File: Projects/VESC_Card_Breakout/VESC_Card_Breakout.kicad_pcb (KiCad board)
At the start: 2 copper layers, 9 parts, among them P1 USB_OTG, P2 CONN_01X02, P3 CONN_01X04, P4 EC90_Flat, P5 CONN_01X02, P6 AMP17614426-2_EDGE, P7 CONN_01X06

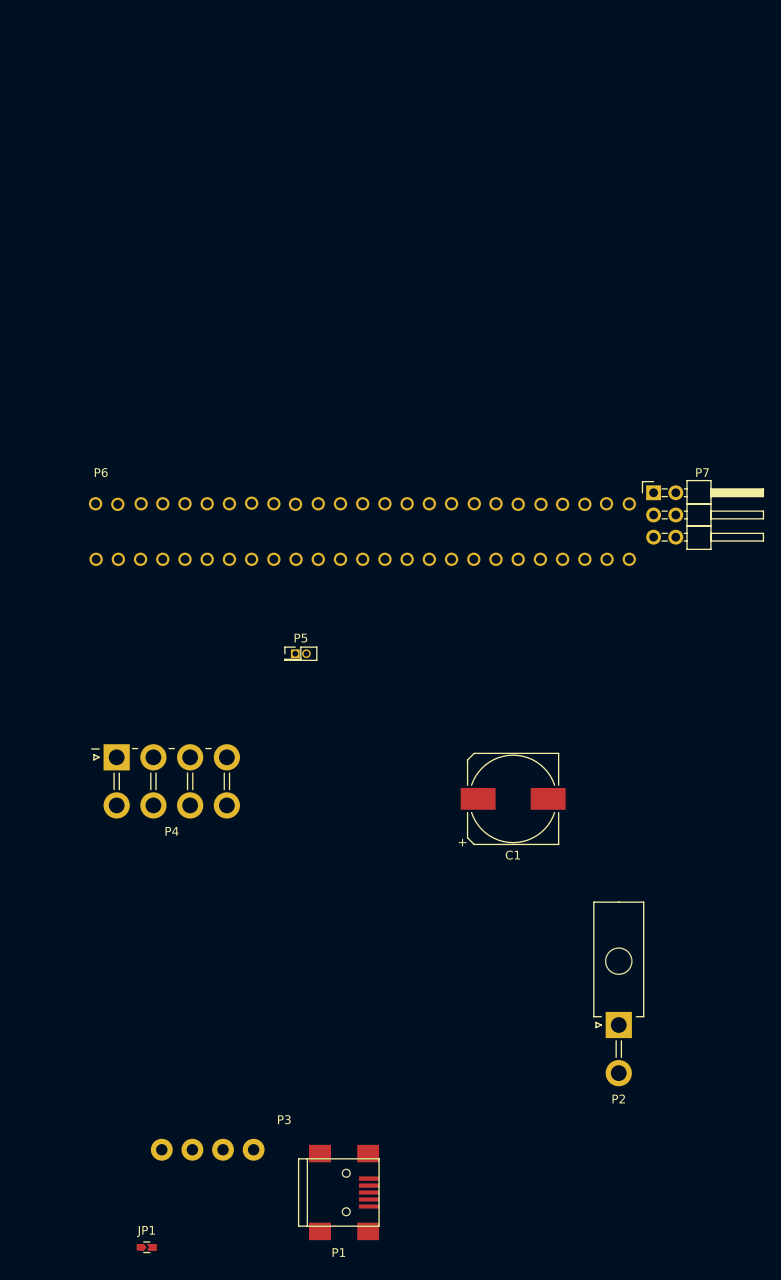
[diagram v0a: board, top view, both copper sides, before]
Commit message: Connected all for VESC_Card_Breakout
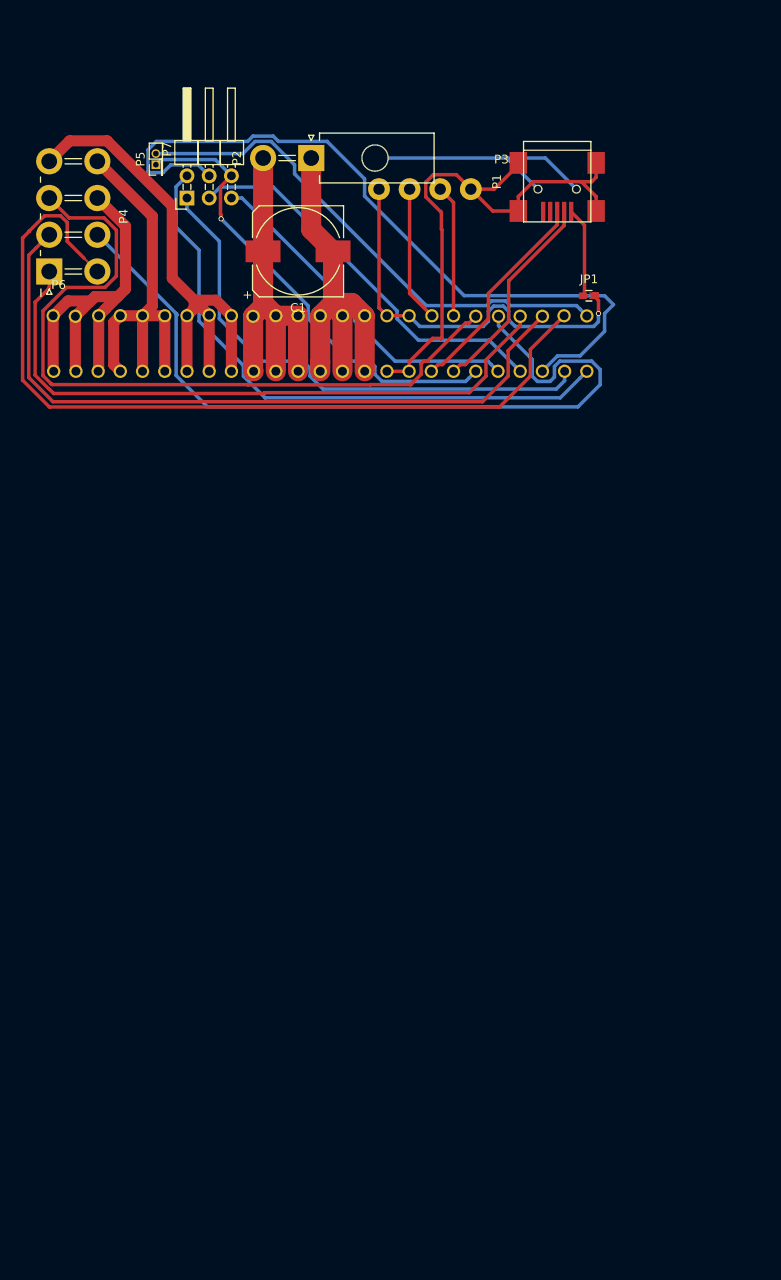
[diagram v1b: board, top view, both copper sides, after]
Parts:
- moved JP1 120.0 mm to (192.8, 58.4)
- moved P1 117.5 mm to (189.1, 46.0), turned to 270 degrees
- moved P3 112.6 mm to (168.8, 46.2)
- moved P2 105.2 mm to (161.0, 42.7), turned to 270 degrees
- moved C1 67.3 mm to (159.5, 53.3)
- moved P7 63.1 mm to (146.8, 47.2), turned to 90 degrees
- moved P5 58.1 mm to (143.3, 43.4), turned to 90 degrees
- moved P4 56.1 mm to (131.1, 55.6), turned to 90 degrees
- moved P6 22.0 mm to (167.1, 74.7)
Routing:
- net /Motor_Controller/H3: track 0.00 -> 99.1 mm
- net Net-(P4-Pad6): track 0.00 -> 91.3 mm
- net Net-(P6-Pad18): track 0.00 -> 85.9 mm
- net Net-(P4-Pad3): track 0.00 -> 85.9 mm
- net /Motor_Controller/H2: track 0.00 -> 82.9 mm
- net /Motor_Controller/H1: track 0.00 -> 74.1 mm
- net /GNDD: track 0.00 -> 72.0 mm
- net Net-(P6-Pad16): track 0.00 -> 68.2 mm
- net Net-(P6-Pad17): track 0.00 -> 60.1 mm
- net Net-(P5-Pad2): track 0.00 -> 59.2 mm
- net /Motor_Controller/Y: track 0.00 -> 58.6 mm
- net /Motor_Controller/GND_AUX: track 0.00 -> 53.8 mm, vias 0 -> 1
- net /Motor_Controller/W: track 0.00 -> 46.6 mm
- net /5v0: track 0.00 -> 46.1 mm, vias 0 -> 1
- net /Motor_Controller/X: track 0.00 -> 45.5 mm
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
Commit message: Rotated component
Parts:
- moved P3 10.4 mm to (178.8, 43.2), turned to 180 degrees
- moved P2 5.08 mm to (161.0, 47.8)
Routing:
- net (no net): track 29.5 -> 0.00 mm
- net /5v0: track 46.1 -> 62.0 mm
- net /Motor_Controller/CANL/RX: track 15.1 -> 25.9 mm
- net /Motor_Controller/PGND: track 44.9 -> 39.6 mm
- net /Motor_Controller/VBAT: track 42.2 -> 37.2 mm
- net /GNDD: track 72.0 -> 77.0 mm
- net /Motor_Controller/CANH/TX: track 15.5 -> 18.2 mm
- net /Motor_Controller/W: track 46.6 -> 44.2 mm
- net Net-(P6-Pad19): track 45.3 -> 46.7 mm
- net Net-(P6-Pad18): track 85.9 -> 84.8 mm
- net Net-(P5-Pad2): track 59.2 -> 58.6 mm

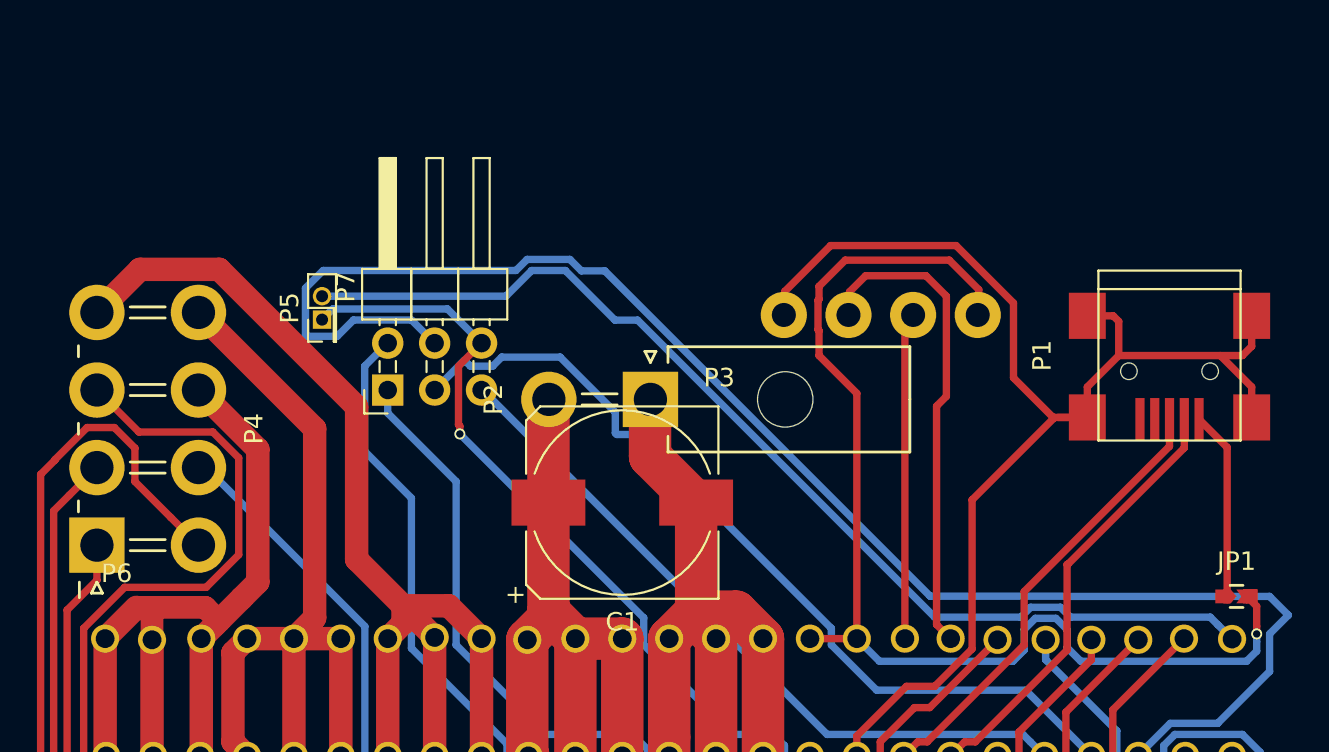
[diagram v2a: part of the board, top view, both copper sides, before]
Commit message: part placement suggestion
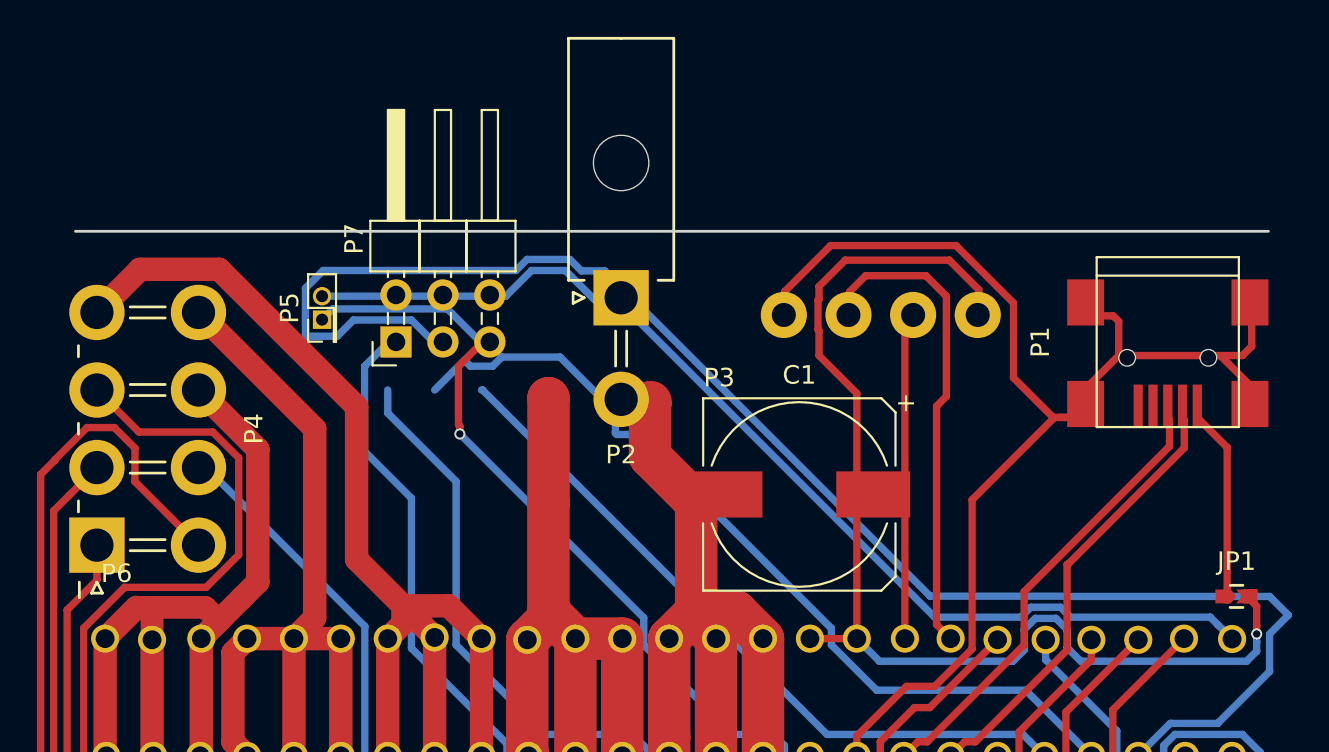
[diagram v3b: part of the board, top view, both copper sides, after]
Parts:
- moved C1 9.60 mm to (169.1, 52.9), turned to 180 degrees
- moved P2 5.73 mm to (159.4, 42.2), turned to 0 degrees
- moved P7 2.64 mm to (147.3, 44.6)
- moved P1 0.73 mm to (189.1, 45.3)
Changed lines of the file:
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@@
-(kicad_pcb (version 4) (host pcbnew 4.0.4-stable)
+(kicad_pcb (version 4) (host pcbnew 4.0.5)
   (general
     (links 64)
     (no_connects 1)
-    (area 116.488999 34.318999 203.923049 75.126)
+    (area 116.488999 34.318999 213.589999 75.126)
     (thickness 1.6)
-    (drawings 2)
+    (drawings 3)
     (tracks 322)
     (zones 0)
@@
   )
   (module Connect:USB_Mini-B (layer F.Cu)
-    (at 189.144 46.028 270)
+    (at 189.05 45.3 270)
     (descr "USB Mini-B 5-pin SMD connector")
     (tags "USB USB_B USB_Mini connector")
@@
   )
   (module Connectors_Molex:Molex_MiniFit-JR-5569-02A2_2x01x4.20mm_Angled (layer F.Cu)
-    (at 161.036 47.752 270)
+    (at 159.45 42.25)
     (descr "Molex Mini-Fit JR, PN:5569-02A2, dual row, side entry type, through hole, with plastic peg mount")
     (tags "connector molex mini-fit 5569")
-    (fp_text reference P2 (at 0 8.5 270) (layer F.SilkS)
-      (effects (font (size 1 1) (thickness 0.15)))
-    )
-    (fp_text value CONN_01X02 (at 0 10 270) (layer F.Fab)
+    (fp_text reference P2 (at 0 8.5) (layer F.SilkS)
+      (effects (font (size 1 1) (thickness 0.15)))
+    )
+    (fp_text value CONN_01X02 (at 0 10) (layer F.Fab)
       (effects (font (size 1 1) (thickness 0.15)))
     )
@@
     (fp_line (start -2.6 0.3) (end -2.6 -0.3) (layer F.SilkS) (width 0.15))
     (fp_line (start -2.6 -0.3) (end -2 0) (layer F.SilkS) (width 0.15))
-    (pad 1 thru_hole rect (at 0 0 270) (size 3 3) (drill 1.8) (layers *.Cu *.Mask)
-      (net 2 /Motor_Controller/PGND))
-    (pad 2 thru_hole circle (at 0 5.5 270) (size 3 3) (drill 1.8) (layers *.Cu *.Mask)
-      (net 1 /Motor_Controller/VBAT))
-    (pad "" np_thru_hole circle (at 0 -7.3 270) (size 3 3) (drill 3) (layers *.Cu))
+    (pad 1 thru_hole rect (at 0 0) (size 3 3) (drill 1.8) (layers *.Cu *.Mask)
+      (net 2 /Motor_Controller/PGND))
+    (pad 2 thru_hole circle (at 0 5.5) (size 3 3) (drill 1.8) (layers *.Cu *.Mask)
+      (net 1 /Motor_Controller/VBAT))
+    (pad "" np_thru_hole circle (at 0 -7.3) (size 3 3) (drill 3) (layers *.Cu))
     (model Connectors_Molex.3dshapes/Molex_MiniFit-JR-5569-02A2_2x01x4.20mm_Angled.wrl
       (at (xyz 0 0 0))
@@
   )
   (module Pin_Headers:Pin_Header_Angled_2x03_Pitch2.54mm (layer F.Cu)
-    (at 146.812 47.244 90)
+    (at 147.26 44.64 90)
     (descr "Through hole angled pin header, 2x03, 2.54mm pitch, 6mm pin length, double rows")
     (tags "Through hole angled pin header THT 2x03 2.54mm double row")
@@
   )
   (module Capacitors_SMD:CP_Elec_10x10 (layer F.Cu)
-    (at 159.512 53.34)
+    (at 169.1 52.9 180)
     (descr "SMT capacitor, aluminium electrolytic, 10x10")
     (attr smd)
-    (fp_text reference C1 (at 0 6.4643) (layer F.SilkS)
-      (effects (font (size 1 1) (thickness 0.15)))
-    )
-    (fp_text value CP (at 0 -6.4643) (layer F.Fab)
+    (fp_text reference C1 (at 0 6.4643 180) (layer F.SilkS)
+      (effects (font (size 1 1) (thickness 0.15)))
+    )
+    (fp_text value CP (at 0 -6.4643 180) (layer F.Fab)
       (effects (font (size 1 1) (thickness 0.15)))
     )
@@
     (fp_line (start -4.3815 -5.0546) (end -5.0546 -4.3815) (layer F.Fab) (width 0.1))
     (fp_line (start 5.0546 -5.0546) (end -4.3815 -5.0546) (layer F.Fab) (width 0.1))
-    (fp_text user + (at -2.9083 -0.0762) (layer F.Fab)
-      (effects (font (size 1 1) (thickness 0.15)))
-    )
-    (fp_text user + (at -5.7785 4.9657) (layer F.SilkS)
+    (fp_text user + (at -2.9083 -0.0762 180) (layer F.Fab)
+      (effects (font (size 1 1) (thickness 0.15)))
+    )
+    (fp_text user + (at -5.7785 4.9657 180) (layer F.SilkS)
       (effects (font (size 1 1) (thickness 0.15)))
     )
@@
     (fp_line (start -5.207 -4.445) (end -4.445 -5.207) (layer F.SilkS) (width 0.12))
     (fp_line (start -4.445 -5.207) (end 5.207 -5.207) (layer F.SilkS) (width 0.12))
-    (pad 1 smd rect (at -4 0 180) (size 4 2.5) (layers F.Cu F.Paste F.Mask)
-      (net 1 /Motor_Controller/VBAT))
-    (pad 2 smd rect (at 4 0 180) (size 4 2.5) (layers F.Cu F.Paste F.Mask)
+    (pad 1 smd rect (at -4 0) (size 4 2.5) (layers F.Cu F.Paste F.Mask)
+      (net 1 /Motor_Controller/VBAT))
+    (pad 2 smd rect (at 4 0) (size 4 2.5) (layers F.Cu F.Paste F.Mask)
       (net 2 /Motor_Controller/PGND))
     (model Capacitors_SMD.3dshapes/CP_Elec_10x10.wrl
@@
     )
   )
+  (gr_line (start 129.9 38.65) (end 194.5 38.65) (layer Edge.Cuts) (width 0.15))
   (dimension 30.48 (width 0.3) (layer Dwgs.User)
     (gr_text "30.480 mm" (at 207.089999 55.88 270) (layer Dwgs.User)

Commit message: Outline lines added in. PCB finished :D
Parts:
- moved P2 1.63 mm to (160.0, 40.7)
- moved P1 1.33 mm to (188.3, 44.2)
- moved C1 1.09 mm to (169.2, 51.8), turned to 0 degrees
- moved P7 0.59 mm to (147.2, 45.2)
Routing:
- net Net-(P4-Pad6): track 91.3 -> 52.5 mm, vias 0 -> 2
- net Net-(P5-Pad2): track 58.6 -> 84.7 mm, vias 0 -> 1
- net Net-(P6-Pad18): track 84.8 -> 62.8 mm, vias 0 -> 1
- net /Motor_Controller/PGND: track 39.6 -> 56.0 mm
- net /Motor_Controller/GND_AUX: track 53.8 -> 66.3 mm, vias 1 -> 0
- net Net-(P6-Pad20): track 39.2 -> 45.9 mm, vias 0 -> 1
- net /Motor_Controller/VBAT: track 37.2 -> 43.2 mm
- net Net-(P6-Pad19): track 46.7 -> 51.8 mm, vias 0 -> 1
- net Net-(P6-Pad16): track 68.2 -> 71.3 mm, vias 0 -> 1
- net Net-(JP1-Pad1): track 10.4 -> 12.6 mm
- net Net-(P6-Pad17): track 60.1 -> 62.1 mm, vias 0 -> 1
- net /Motor_Controller/CANH/TX: track 18.2 -> 19.7 mm
- net /Motor_Controller/USBDM: track 23.8 -> 25.3 mm
- net /Motor_Controller/USBDP: track 24.5 -> 26.0 mm
- net /GNDD: track 77.0 -> 76.1 mm
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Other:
- board outline added: 67.1 x 33.5 mm

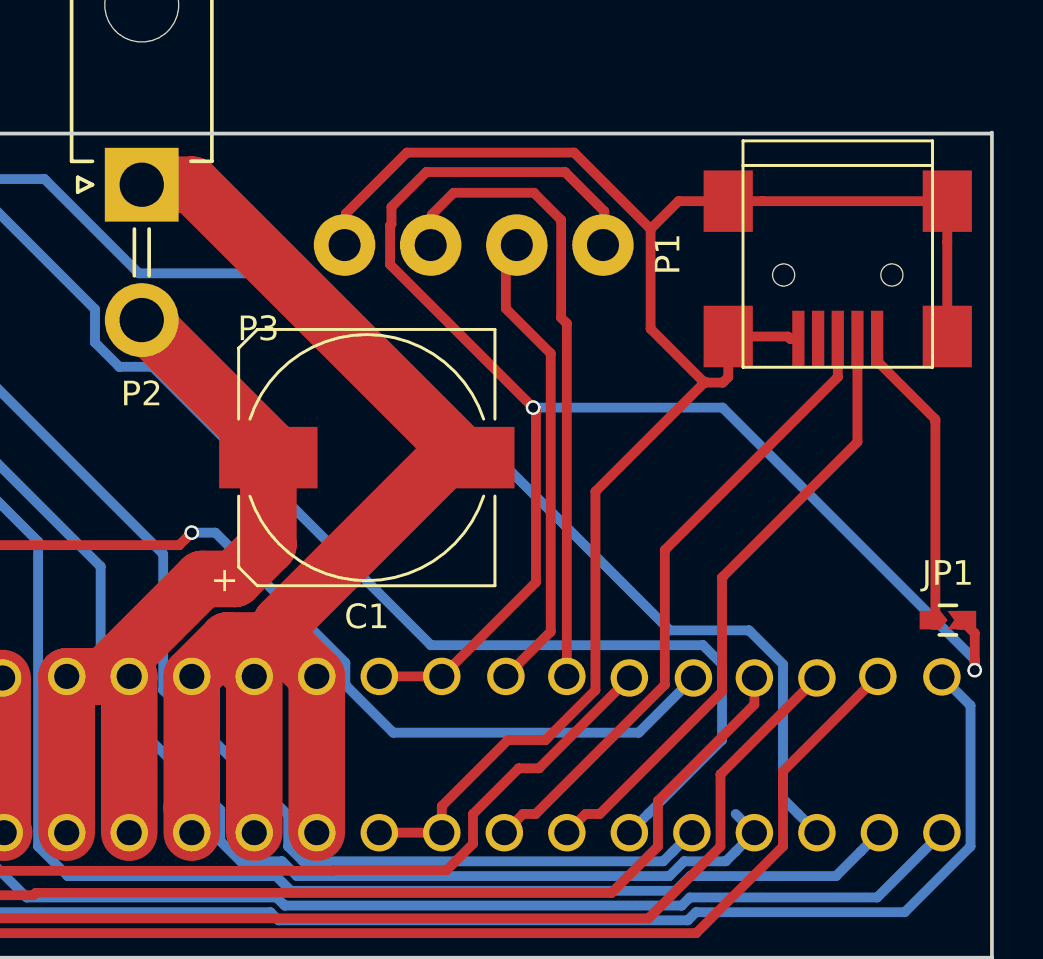
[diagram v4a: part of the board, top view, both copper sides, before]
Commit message: finished reconnecting stuff on VESC
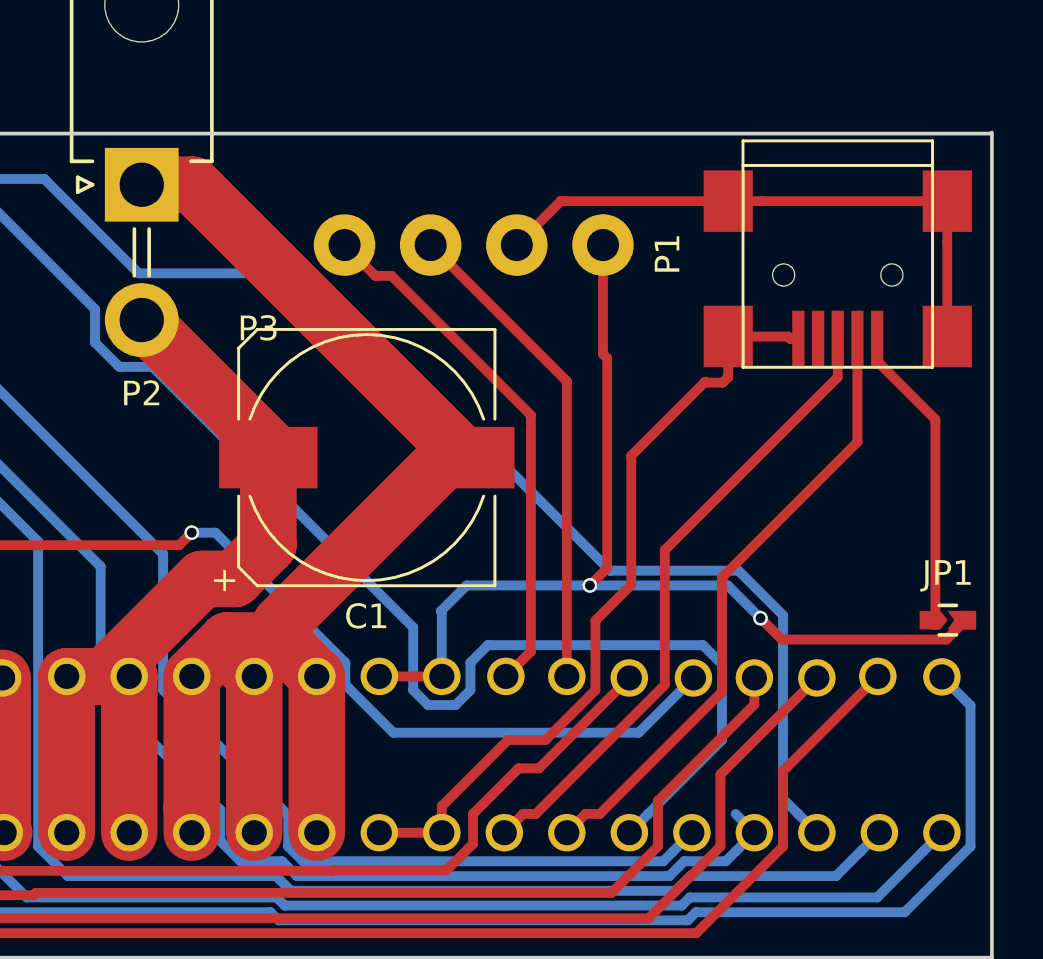
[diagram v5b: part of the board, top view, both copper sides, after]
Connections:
- P1 pad 4: Net-(P1-Pad4) -> (no net)
- P3 pad 2: /Motor_Controller/CANH/TX -> /GNDD
- P3 pad 4: /GNDD -> /Motor_Controller/CANH/TX
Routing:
- net /5v0: track 61.3 -> 43.8 mm
- net /GNDD: track 76.1 -> 59.9 mm
- net /Motor_Controller/CANL/RX: track 25.4 -> 19.8 mm
- net /Motor_Controller/GND_AUX: track 66.3 -> 70.5 mm
- net /Motor_Controller/CANH/TX: track 19.7 -> 21.5 mm
- net Net-(P6-Pad18): track 62.8 -> 64.0 mm

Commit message: sync for working with liz
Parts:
- added G***: LOGO, USST-footprints:USSTLOGO, B.Cu at (179.5, 51.0)
- added G***: LOGO, USST-footprints:OSH_PARK_LOGO_SM, B.Cu at (150.4, 55.8)
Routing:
- net /Motor_Controller/W: track 44.2 -> 52.1 mm
- net /Motor_Controller/VBAT: track 43.2 -> 50.9 mm
- net /GNDD: track 59.9 -> 66.2 mm
- net /Motor_Controller/Y: track 58.5 -> 64.2 mm
- net /Motor_Controller/X: track 45.5 -> 50.8 mm
- net /Motor_Controller/PGND: track 56.0 -> 61.0 mm
- net Net-(P4-Pad6): track 52.5 -> 54.3 mm
- net Net-(P4-Pad3): track 85.9 -> 87.1 mm
- net /Motor_Controller/H3: track 98.9 -> 100.0 mm
- net Net-(P6-Pad19): track 51.8 -> 50.8 mm
- net /Motor_Controller/H1: track 74.1 -> 75.2 mm
- net /Motor_Controller/H2: track 82.9 -> 83.7 mm
- net Net-(P6-Pad20): track 45.9 -> 45.3 mm
- net /Motor_Controller/GND_AUX: track 70.5 -> 69.9 mm
- added copper zone on B.Cu, net /Motor_Controller/PGND
- added copper zone on F.Cu, net /Motor_Controller/PGND
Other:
- outline, holes or cut-outs redrawn
- board text added: "2017 Liza Catambing"
- board text added: "VESC-R Breakout"
